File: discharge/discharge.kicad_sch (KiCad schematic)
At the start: 8 parts, among them J1 Conn_SDC, J2 Conn_HV_IN, J3 Conn_HV_OUT, K1 5503-12-1

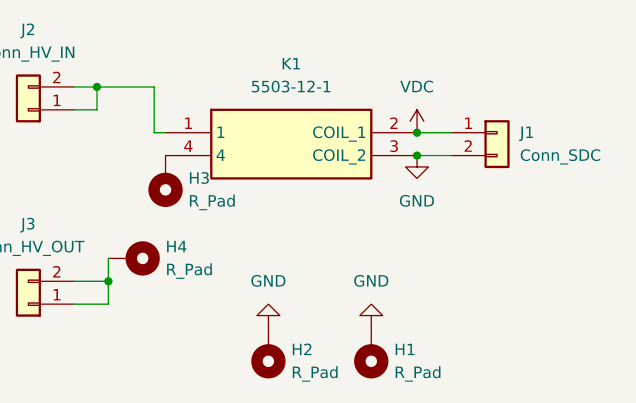
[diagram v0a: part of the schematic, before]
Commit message: chore: reduce board size and increase trace width
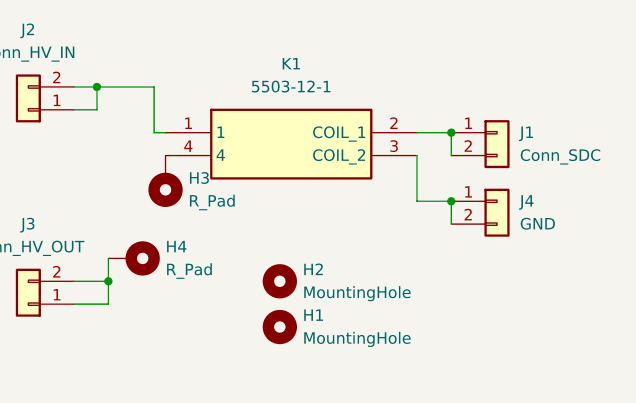
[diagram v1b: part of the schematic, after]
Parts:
- removed H1, H2: R_Pad, MountingHole:MountingHole_4.3mm_M4_Pad, symbol 178.6164.0001:MountingHole_Pad
- added H1, H2: MountingHole, MountingHole:MountingHole_3.2mm_M3, symbol Mechanical:MountingHole
- added J4: GND, Connector_JST:JST_XH_B2B-XH-A_1x02_P2.50mm_Vertical, symbol 178.6164.0001:Conn_01x02
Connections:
- net VDC is gone; now on an unnamed net: J1.1 (Pin_1), K1.2 (COIL_1)
- net GND: no longer names the net of J1.2 (Pin_2)
- net GND: no longer K1.3 (COIL_2)
- new net: J4.1 (Pin_1), J4.2 (Pin_2), K1.3 (COIL_2)

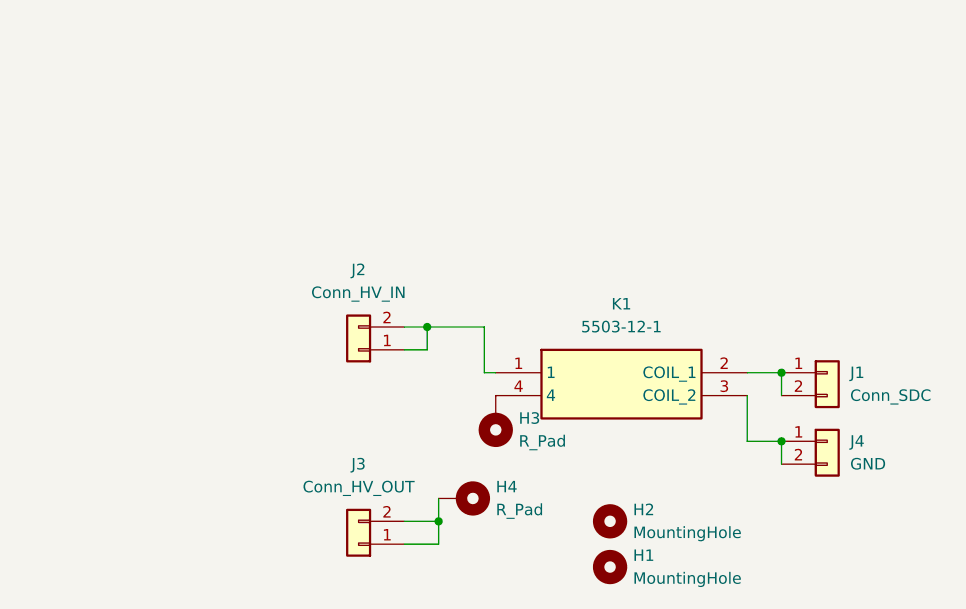
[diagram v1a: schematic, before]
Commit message: feat: combine 2 disC into PCB
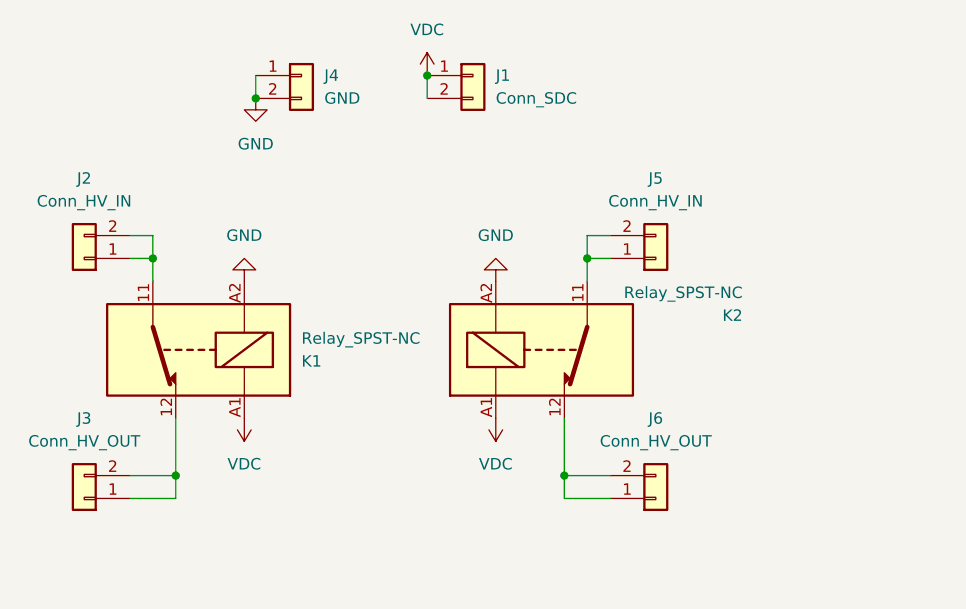
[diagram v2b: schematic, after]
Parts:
- removed H1, H2: MountingHole, MountingHole:MountingHole_3.2mm_M3, symbol Mechanical:MountingHole
- removed H3, H4: R_Pad, MountingHole:MountingHole_4.3mm_M4_Pad, symbol 178.6164.0001:MountingHole_Pad
- removed K1: 5503-12-1, 5503121, symbol 5503-12-1:5503-12-1
- added J5: Conn_HV_IN, Connector_Molex:Molex_Micro-Fit_3.0_43650-0200_1x02_P3.00mm_Horizontal, symbol 178.6164.0001:Conn_01x02
- added J6: Conn_HV_OUT, Connector_Molex:Molex_Micro-Fit_3.0_43650-0200_1x02_P3.00mm_Horizontal, symbol 178.6164.0001:Conn_01x02
- added K1, K2: Relay_SPST-NC, Reed:Reed, symbol Relay:Relay_SPST-NC
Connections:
- net at J2.1 (Pin_1), J2.2 (Pin_2): now also K1.11
- net VDC: now reaches J1.1 (Pin_1), J1.2 (Pin_2)
- net VDC: now also K1.A1, K2.A1
- net GND: now reaches J4.1 (Pin_1), J4.2 (Pin_2)
- net GND: now also K1.A2, K2.A2
- net at J3.1 (Pin_1), J3.2 (Pin_2): now also K1.12
- new net: J6.1 (Pin_1), J6.2 (Pin_2), K2.12
- new net: J5.1 (Pin_1), J5.2 (Pin_2), K2.11
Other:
- moved on the sheet: J1, J2, J3, J4

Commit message: add timer
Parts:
- added C1, C3, C4: 100n, Capacitor_SMD:C_0603_1608Metric, symbol Device:C_Small
- added C2: 100u, Capacitor_SMD:C_0603_1608Metric, symbol Device:C_Small
- added C5, C6: 1u, Capacitor_SMD:C_0603_1608Metric, symbol Device:C_Small
- added D1: D_Small, Diode_SMD:D_SOD-123F, symbol Device:D_Small
- added J7: Conn, Connector_JST:JST_XH_B2B-XH-A_1x02_P2.50mm_Vertical, symbol 178.6164.0001:Conn_01x02
- added K3: JY-12H-K, JY12HK, symbol JY-12H-K:JY-12H-K
- added Q2: Si2301CDS, Package_TO_SOT_SMD:SOT-23, symbol PCM_Transistor_MOSFET_AKL:Si2301CDS
- added R1: 4.7k, Resistor_SMD:R_0603_1608Metric, symbol Device:R_Small
- added R2: 68k, Resistor_SMD:R_0603_1608Metric, symbol Device:R_Small
- added R4, R5: 10k, Resistor_SMD:R_0603_1608Metric, symbol Device:R_Small
- added U1: SE555D, Package_SO:SOIC-8_3.9x4.9mm_P1.27mm, symbol Timer:SE555D
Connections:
- net GND: now also C1.2, C2.2, C3.1, C4.1, C5.2, C6.2, D1.2 (A), K3.9 (COIL_2), Q2.3 (D), U1.1 (GND)
- net VDC: now also C5.1, C6.1, D1.1 (K), K3.8 (COIL_1), Q2.2 (S), R2.1, R4.1, R5.1, U1.8 (VCC)
- new net: R1.1, R2.2
- new net: C3.2, C4.2, R5.2, U1.2 (TR)
- new net: J7.1 (Pin_1), K3.16 (COM)
- new net: J7.2 (Pin_2), K3.13 (NO)
- new net: C1.1, U1.5 (CV)
- new net: C2.1, R1.2, U1.6 (THR), U1.7 (DIS)
- new net +12V: U1.4 (R)
- new net Timer: Q2.1 (G), R4.2, U1.3 (Q)

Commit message: finish timer layout
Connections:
- net +12V: now also R4.1; no longer U1.4 (R)
- net VDC: now also U1.4 (R); no longer R4.1
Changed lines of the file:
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@@
+	)
+	(symbol
+		(lib_id "power:+12V")
+		(at 25.4 111.76 0)
+		(unit 1)
+		(exclude_from_sim no)
+		(in_bom yes)
+		(on_board yes)
+		(dnp no)
+		(fields_autoplaced yes)
+		(property "Reference" "#PWR10"
+			(at 25.4 115.57 0)
+			(effects
+				(font
+					(size 1.27 1.27)
+				)
+				(hide yes)
+			)
+		)
+		(property "Value" "+12V"
+			(at 25.4 106.68 0)
+			(effects
+				(font
+					(size 1.27 1.27)
+				)
+			)
+		)
+		(property "Footprint" ""
+			(at 25.4 111.76 0)
+			(effects
+				(font
+					(size 1.27 1.27)
+				)
+				(hide yes)
+			)
+		)
+		(property "Datasheet" ""
+			(at 25.4 111.76 0)
+			(effects
+				(font
+					(size 1.27 1.27)
+				)
+				(hide yes)
+			)
+		)
+		(property "Description" ""
+			(at 25.4 111.76 0)
+			(effects
+				(font
+					(size 1.27 1.27)
+				)
+				(hide yes)
+			)
+		)
+		(pin "1"
+		)
+		(instances
+			(project "discharge"
+				(path "/40e51e17-8a47-4b70-900c-c1c667ec5378"
+					(reference "#PWR10")
+					(unit 1)
+				)
+			)
+		)
 	)
 	(symbol
@@
 				(path "/40e51e17-8a47-4b70-900c-c1c667ec5378"
 					(reference "#PWR02")
-					(unit 1)
-				)
-			)
-		)
-	)
-	(symbol
-		(lib_id "power:+12V")
-		(at 44.45 116.84 0)
-		(unit 1)
-		(exclude_from_sim no)
-		(in_bom yes)
-		(on_board yes)
-		(dnp no)
-		(fields_autoplaced yes)
-		(property "Reference" "#PWR10"
-			(at 44.45 120.65 0)
-			(effects
-				(font
-					(size 1.27 1.27)
-				)
-				(hide yes)
-			)
-		)
-		(property "Value" "+12V"
-			(at 44.45 111.76 0)
-			(effects
-				(font
-					(size 1.27 1.27)
-				)
-			)
-		)
-		(property "Footprint" ""
-			(at 44.45 116.84 0)
-			(effects
-				(font
-					(size 1.27 1.27)
-				)
-				(hide yes)
-			)
-		)
-		(property "Datasheet" ""
-			(at 44.45 116.84 0)
-			(effects
-				(font
-					(size 1.27 1.27)
-				)
-				(hide yes)
-			)
-		)
-		(property "Description" ""
-			(at 44.45 116.84 0)
-			(effects
-				(font
-					(size 1.27 1.27)
-				)
-				(hide yes)
-			)
-		)
-		(pin "1"
-		)
-		(instances
-			(project "discharge"
-				(path "/40e51e17-8a47-4b70-900c-c1c667ec5378"
-					(reference "#PWR10")
 					(unit 1)
 				)
@@
 	)
 	(symbol
+		(lib_id "power:VDC")
+		(at 44.45 116.84 0)
+		(mirror y)
+		(unit 1)
+		(exclude_from_sim no)
+		(in_bom yes)
+		(on_board yes)
+		(dnp no)
+		(fields_autoplaced yes)
+		(property "Reference" "#PWR8"
+			(at 44.45 120.65 0)
+			(effects
+				(font
+					(size 1.27 1.27)
+				)
+				(hide yes)
+			)
+		)
+		(property "Value" "VDC"
+			(at 44.45 111.9185 0)
+			(effects
+				(font
+					(size 1.27 1.27)
+				)
+			)
+		)
+		(property "Footprint" ""
+			(at 44.45 116.84 0)
+			(effects
+				(font
+					(size 1.27 1.27)
+				)
+				(hide yes)
+			)
+		)
+		(property "Datasheet" ""
+			(at 44.45 116.84 0)
+			(effects
+				(font
+					(size 1.27 1.27)
+				)
+				(hide yes)
+			)
+		)
+		(property "Description" "Power symbol creates a global label with name \"VDC\""
+			(at 44.45 116.84 0)
+			(effects
+				(font
+					(size 1.27 1.27)
+				)
+				(hide yes)
+			)
+		)
+		(pin "1"
+		)
+		(instances
+			(project "discharge"
+				(path "/40e51e17-8a47-4b70-900c-c1c667ec5378"
+					(reference "#PWR8")
+					(unit 1)
+				)
+			)
+		)
+	)
+	(symbol
 		(lib_id "178.6164.0001:Conn_01x02")
 		(at 55.88 71.12 180)
@@
 					(unit 1)
 				)
-			)
-		)
-	)
-	(symbol
-		(lib_id "power:VDC")
-		(at 25.4 111.76 0)
-		(mirror y)
-		(unit 1)
-		(exclude_from_sim no)
-		(in_bom yes)
-		(on_board yes)
-		(dnp no)
-		(fields_autoplaced yes)
-		(property "Reference" "#PWR8"
-			(at 25.4 115.57 0)
-			(effects
-				(font
-					(size 1.27 1.27)
-				)
-				(hide yes)
-			)
-		)
-		(property "Value" "VDC"
-			(at 25.4 106.8385 0)
-			(effects
-				(font
-					(size 1.27 1.27)
-				)
-			)
-		)
-		(property "Footprint" ""
-			(at 25.4 111.76 0)
-			(effects
-				(font
-					(size 1.27 1.27)
-				)
-				(hide yes)
-			)
-		)
-		(property "Datasheet" ""
-			(at 25.4 111.76 0)
-			(effects
-				(font
-					(size 1.27 1.27)
-				)
-				(hide yes)
-			)
-		)
-		(property "Description" "Power symbol creates a global label with name \"VDC\""
-			(at 25.4 111.76 0)
-			(effects
-				(font
-					(size 1.27 1.27)
-				)
-				(hide yes)
-			)
-		)
-		(pin "1"
-		)
-		(instances
-			(project "discharge"
-				(path "/40e51e17-8a47-4b70-900c-c1c667ec5378"
-					(reference "#PWR8")
-					(unit 1)
-				)

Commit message: modify discharge ver2
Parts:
- removed C3, C4: 100n, Capacitor_SMD:C_0603_1608Metric, symbol Device:C_Small
- removed C5: 1u, Capacitor_SMD:C_0603_1608Metric, symbol Device:C_Small
- removed Q2: Si2301CDS, Package_TO_SOT_SMD:SOT-23, symbol PCM_Transistor_MOSFET_AKL:Si2301CDS
- removed R5: 10k, Resistor_SMD:R_0603_1608Metric, symbol Device:R_Small
- added Q1: Si2301CDS, Package_TO_SOT_SMD:SOT-23, symbol PCM_Transistor_MOSFET_AKL:Si2301CDS
- C2: value 100u -> 22u; footprint Capacitor_SMD:C_0603_1608Metric -> Capacitor_SMD:C_0805_2012Metric
- D1: value D_Small -> 1N4148W-7-F
- R1: value 4.7k -> 47k
- R2: value 68k -> 280k
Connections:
- net +12V is gone; now on net VDC: R4.1
- net GND: now also U1.2 (TR), U1.7 (DIS), Q1.3 (D); no longer K3.9 (COIL_2)
- net Timer: now also Q1.1 (G)
- net VDC: no longer D1.1 (K)
- net at C2.1, R1.2, U1.6 (THR): no longer U1.7 (DIS)
- new net: D1.1 (K), K3.9 (COIL_2), Q1.2 (S)

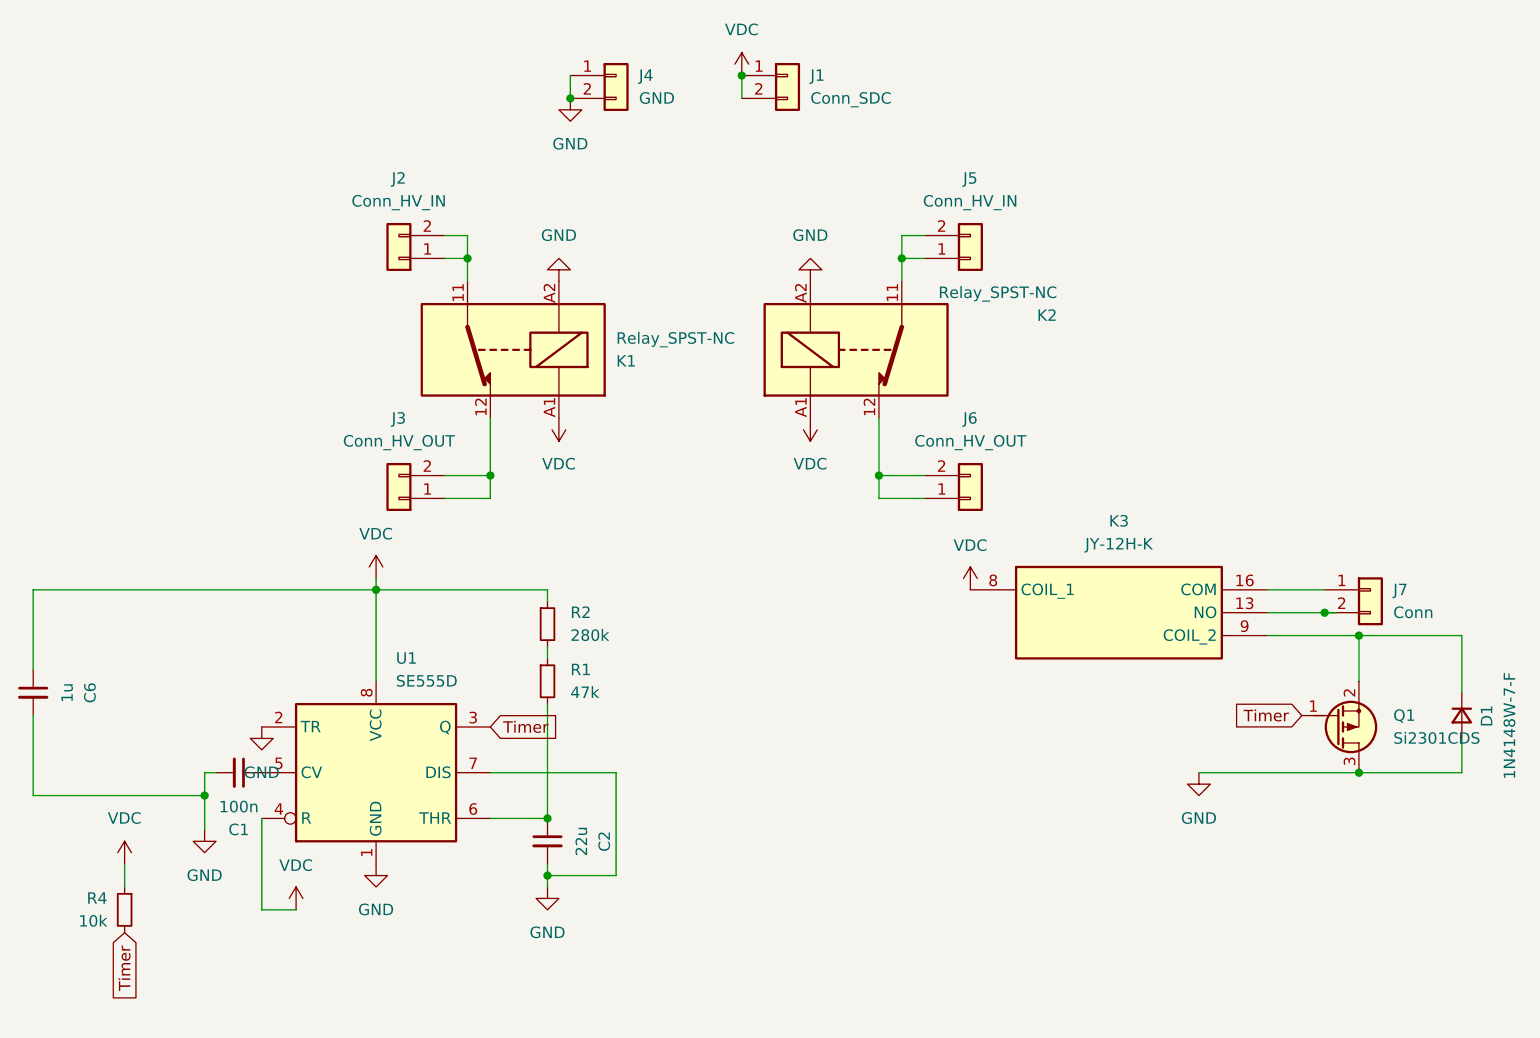
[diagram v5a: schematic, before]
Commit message: fix: move flyback diode position
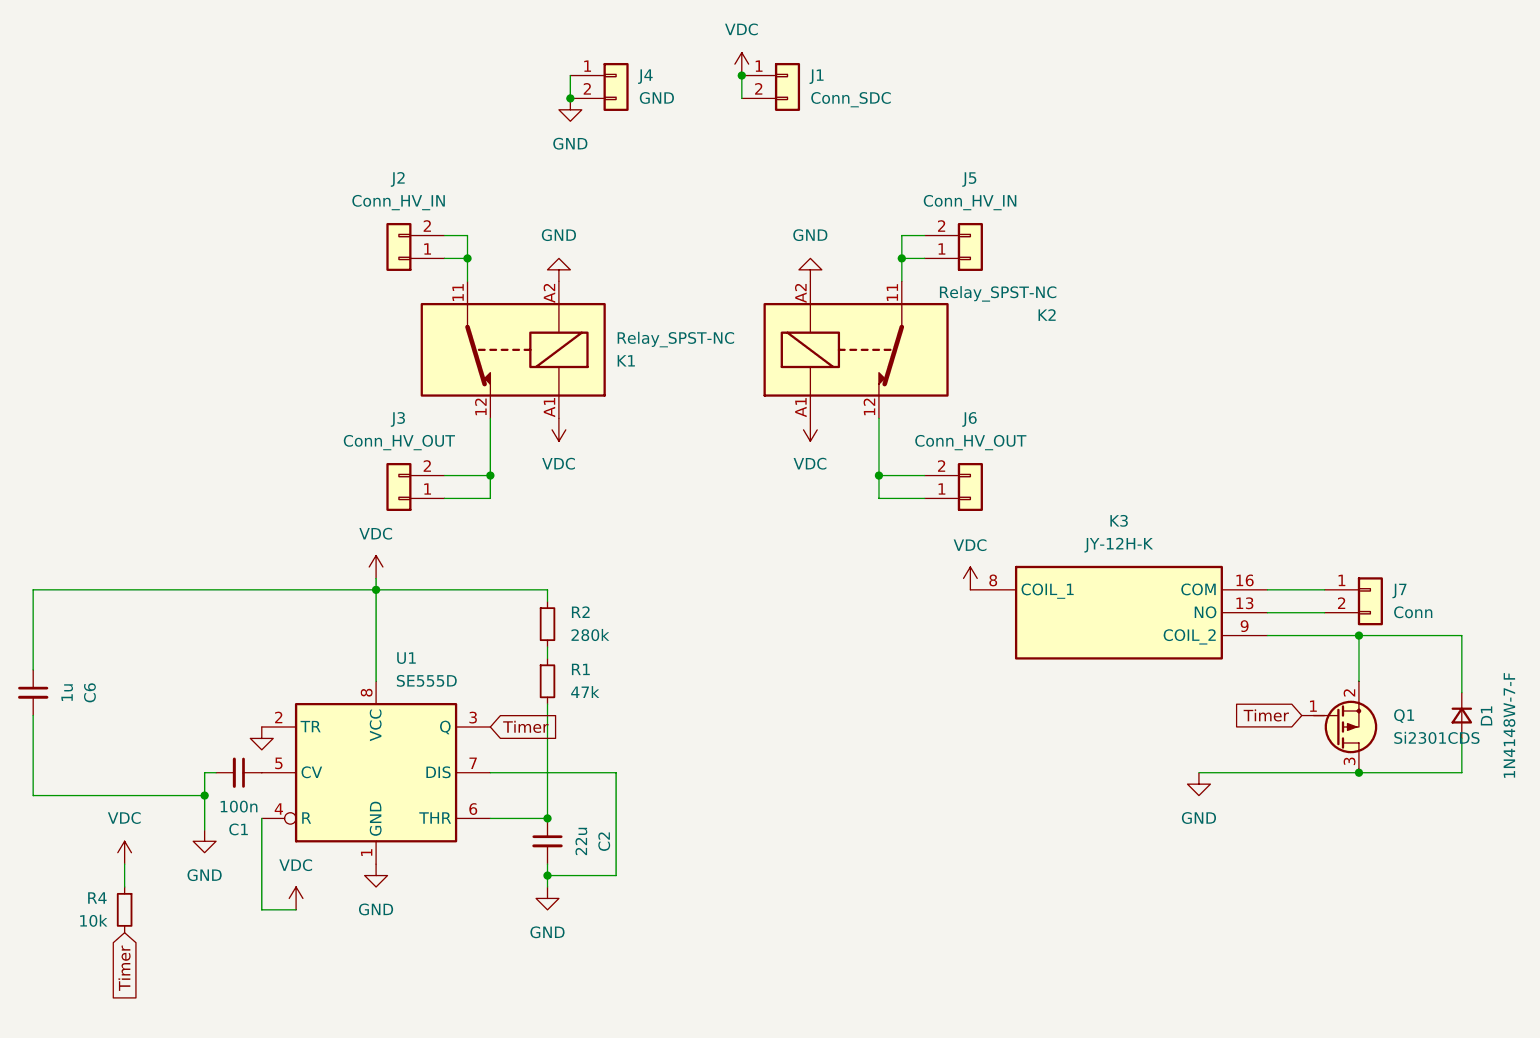
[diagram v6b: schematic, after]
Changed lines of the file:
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@@
-	)
-	(junction
-		(at 158.75 83.82)
-		(diameter 0)
-		(color 0 0 0 0)
 	)
 	(junction
@@
 		(pts
 			(xy 173.99 92.71) (xy 173.99 86.36)
-		)
-		(stroke
-			(width 0)
-			(type default)
-		)
-	)
-	(wire
-		(pts
-			(xy 160.02 83.82) (xy 158.75 83.82)
 		)
 		(stroke
@@
 		(on_board yes)
 		(dnp no)
-		(fields_autoplaced yes)
 		(property "Reference" "#PWR15"
 			(at 40.64 102.87 0)
@@
 		)
 		(property "Value" "GND"
-			(at 40.64 101.6 0)
-			(effects
-				(font
-					(size 1.27 1.27)
-				)
-			)
-		)
+			(at 37.592 97.79 0)
+			(effects
+				(font
+					(size 1.27 1.27)
+				)
+				(hide yes)
+			)
+		)
